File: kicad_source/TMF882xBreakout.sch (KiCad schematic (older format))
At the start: 27 parts, among them CN1 CONN_01X06, CN2 CONN_01X07, CN3 SM05B-SRSS-TB, CN4 SM05B-SRSS-TB, Q1 BSS138, Q2 BSS138, Q3 BSS138, U1 MIC5225-3.3, U2 TMF8801

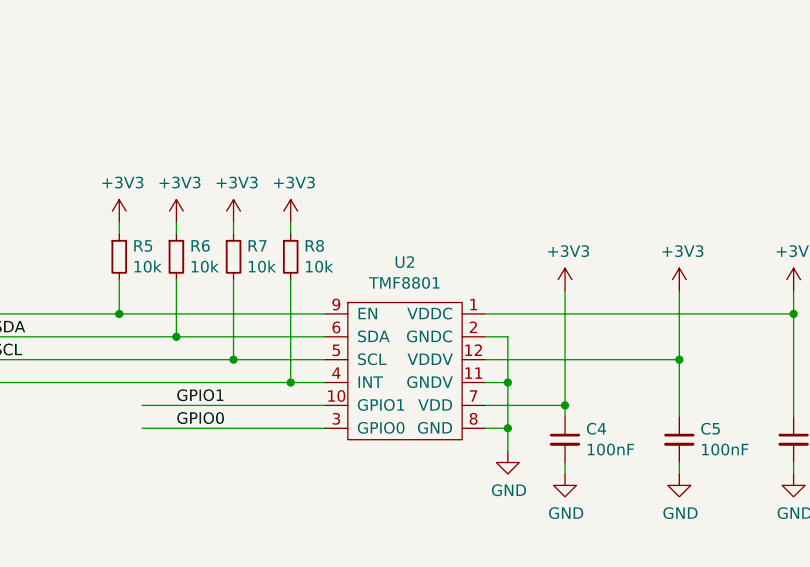
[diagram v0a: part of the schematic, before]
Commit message: updated project, added footprint for TMF882x
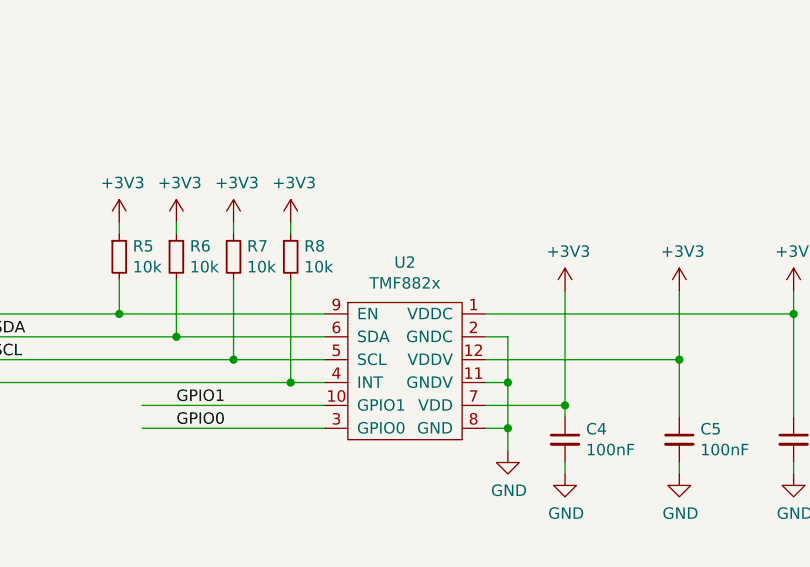
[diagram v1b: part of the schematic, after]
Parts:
- removed U2: TMF8801, IC_sensor:TMF8801, symbol IC_sensor:TMF8801
- added U2: TMF882x, IC_sensor:TMF882x, symbol IC_sensor:TMF882x
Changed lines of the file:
@@
 encoding utf-8
 Sheet 1 1
-Title "TMF8801Breakout"
-Date "2020-11-27"
+Title "TMF882xBreakout"
+Date "2022-01-04"
 Rev "0.1"
 Comp "genrationmake"
@@
 Comment4 ""
 $EndDescr
-$Comp
-L IC_sensor:TMF8801 U2
-U 1 1 5FB709E7
-P 5950 2250
-F 0 "U2" H 5950 2725 50  0000 C CNN
-F 1 "TMF8801" H 5950 2634 50  0000 C CNN
-F 2 "IC_sensor:TMF8801" H 5950 2250 50  0001 C CNN
-F 3 "" H 5950 2250 50  0001 C CNN
-	1    5950 2250
-	1    0    0    -1
-$EndComp
 $Comp
 L power-supply:GND #PWR021
@@
 Wire Wire Line
 	4800 2500 5600 2500
+$Comp
+L IC_sensor:TMF882x U2
+U 1 1 61D45030
+P 5950 2250
+F 0 "U2" H 5950 2725 50  0000 C CNN
+F 1 "TMF882x" H 5950 2634 50  0000 C CNN
+F 2 "IC_sensor:TMF882x" H 5950 2250 50  0001 C CNN
+F 3 "" H 5950 2250 50  0001 C CNN
+	1    5950 2250
+	1    0    0    -1
+$EndComp
 $EndSCHEMATC
